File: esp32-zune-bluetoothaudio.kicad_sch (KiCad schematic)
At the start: 21 parts

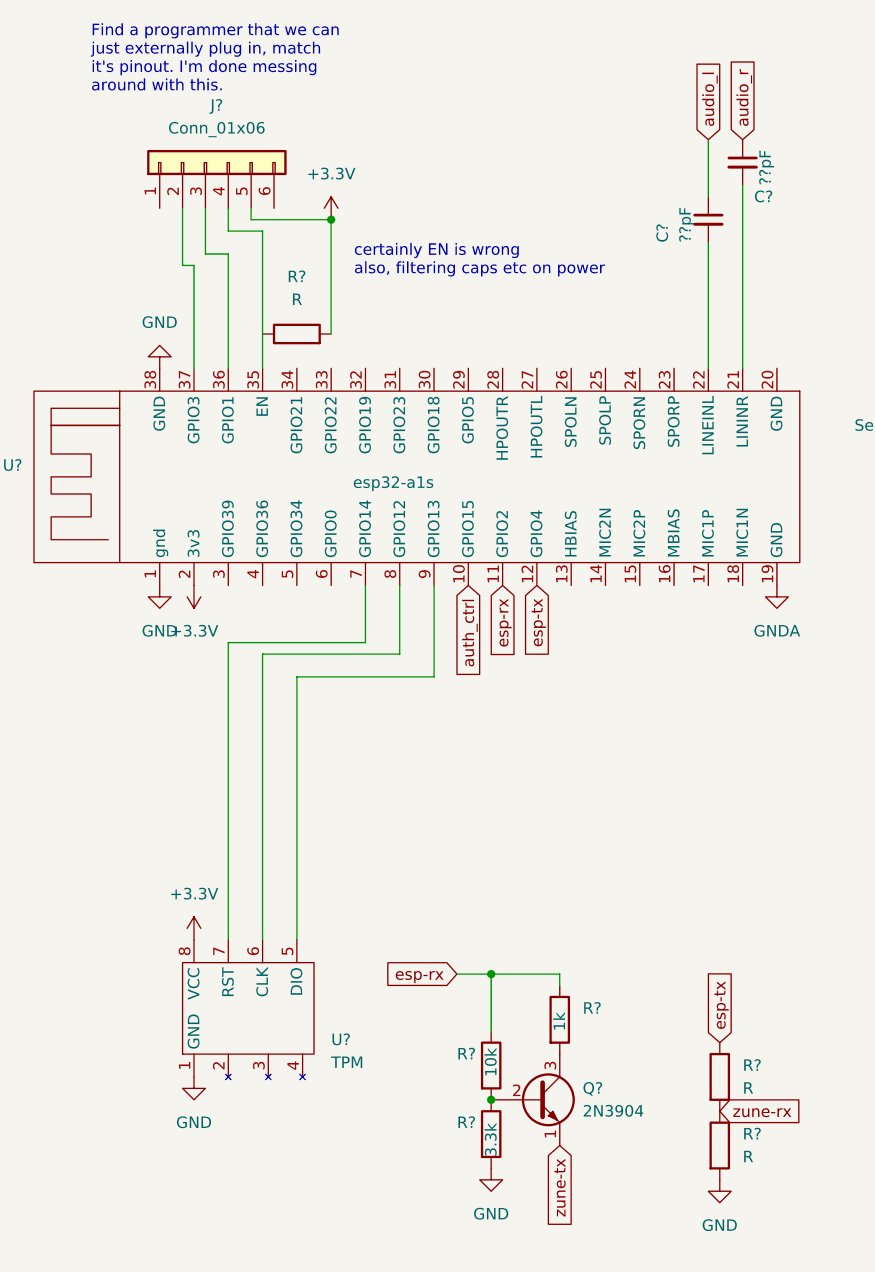
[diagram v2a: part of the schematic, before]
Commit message: starting to write a zune "driver", updating schematic to match breadboard. I'm getting close to laying out a pcb.
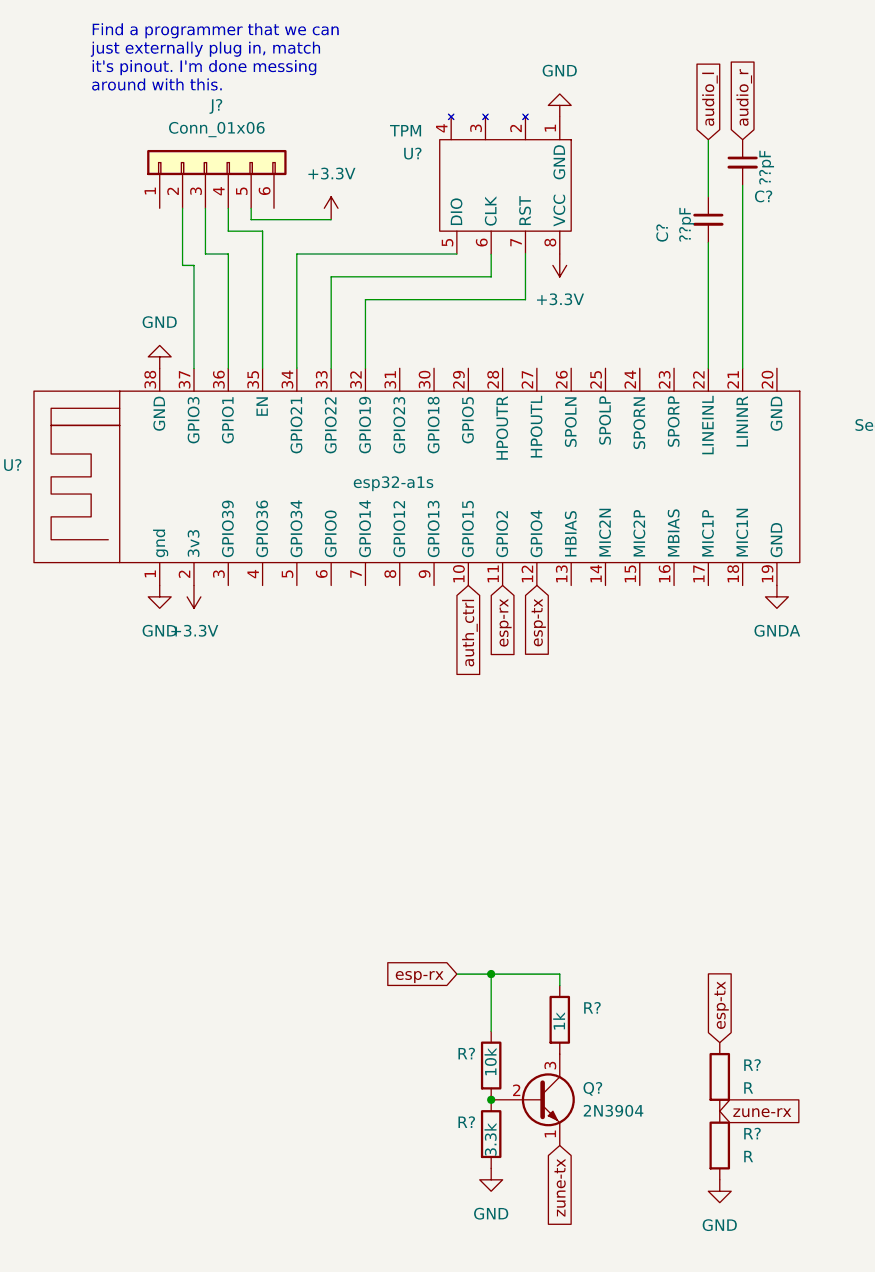
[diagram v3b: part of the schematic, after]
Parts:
- removed R?: R, symbol Device:R
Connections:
- net at U?.5 (DIO): now also U?.34 (GPIO21); no longer U?.9 (GPIO13)
- net at U?.6 (CLK): now also U?.33 (GPIO22); no longer U?.8 (GPIO12)
- net at U?.7 (RST): now also U?.32 (GPIO19); no longer U?.7 (GPIO14)
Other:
- note removed: "certainly EN is wrong also, filtering caps etc on power"
- moved on the sheet: U?
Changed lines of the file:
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@@
   (junction (at 142.24 115.57) (diameter 0) (color 0 0 0 0)
   )
-  (junction (at 52.07 41.91) (diameter 0) (color 0 0 0 0)
-  )
   (junction (at 233.68 101.6) (diameter 0) (color 0 0 0 0)
   )
   (junction (at 232.41 99.06) (diameter 0) (color 0 0 0 0)
   )
-  (wire (pts (xy 52.07 41.91) (xy 52.07 54.61))
-    (stroke (width 0) (type default) (color 0 0 0 0))
-  )
   (wire (pts (xy 69.85 125.73) (xy 69.85 132.08))
     (stroke (width 0) (type default) (color 0 0 0 0))
@@
     (stroke (width 0) (type default) (color 0 0 0 0))
   )
-  (wire (pts (xy 55.88 88.9) (xy 40.64 88.9))
-    (stroke (width 0) (type default) (color 0 0 0 0))
-  )
-  (wire (pts (xy 48.26 121.92) (xy 48.26 92.71))
+  (wire (pts (xy 69.85 48.26) (xy 52.07 48.26))
     (stroke (width 0) (type default) (color 0 0 0 0))
   )
@@
     (stroke (width 0) (type default) (color 0 0 0 0))
   )
-  (wire (pts (xy 44.45 90.17) (xy 59.69 90.17))
-    (stroke (width 0) (type default) (color 0 0 0 0))
-  )
-  (wire (pts (xy 55.88 82.55) (xy 55.88 88.9))
-    (stroke (width 0) (type default) (color 0 0 0 0))
-  )
   (wire (pts (xy 166.37 45.72) (xy 173.99 45.72))
     (stroke (width 0) (type default) (color 0 0 0 0))
@@
     (stroke (width 0) (type default) (color 0 0 0 0))
   )
+  (wire (pts (xy 73.66 50.8) (xy 55.88 50.8))
+    (stroke (width 0) (type default) (color 0 0 0 0))
+  )
   (wire (pts (xy 234.95 43.18) (xy 233.68 43.18))
     (stroke (width 0) (type default) (color 0 0 0 0))
   )
+  (wire (pts (xy 48.26 45.72) (xy 48.26 58.42))
+    (stroke (width 0) (type default) (color 0 0 0 0))
+  )
   (wire (pts (xy 217.17 88.9) (xy 217.17 91.44))
     (stroke (width 0) (type default) (color 0 0 0 0))
@@
     (stroke (width 0) (type default) (color 0 0 0 0))
   )
-  (wire (pts (xy 48.26 92.71) (xy 63.5 92.71))
+  (wire (pts (xy 55.88 50.8) (xy 55.88 58.42))
     (stroke (width 0) (type default) (color 0 0 0 0))
   )
@@
     (stroke (width 0) (type default) (color 0 0 0 0))
   )
-  (wire (pts (xy 59.69 90.17) (xy 59.69 82.55))
+  (wire (pts (xy 66.04 45.72) (xy 48.26 45.72))
     (stroke (width 0) (type default) (color 0 0 0 0))
   )
@@
     (stroke (width 0) (type default) (color 0 0 0 0))
   )
+  (wire (pts (xy 69.85 45.72) (xy 69.85 48.26))
+    (stroke (width 0) (type default) (color 0 0 0 0))
+  )
   (wire (pts (xy 228.6 45.72) (xy 228.6 48.26))
     (stroke (width 0) (type default) (color 0 0 0 0))
@@
     (stroke (width 0) (type default) (color 0 0 0 0))
   )
-  (wire (pts (xy 63.5 92.71) (xy 63.5 82.55))
-    (stroke (width 0) (type default) (color 0 0 0 0))
-  )
   (wire (pts (xy 44.45 43.18) (xy 40.64 43.18))
     (stroke (width 0) (type default) (color 0 0 0 0))
@@
     (stroke (width 0) (type default) (color 0 0 0 0))
   )
-  (wire (pts (xy 44.45 121.92) (xy 44.45 90.17))
-    (stroke (width 0) (type default) (color 0 0 0 0))
-  )
   (wire (pts (xy 233.68 101.6) (xy 232.41 101.6))
     (stroke (width 0) (type default) (color 0 0 0 0))
@@
     (stroke (width 0) (type default) (color 0 0 0 0))
   )
-  (wire (pts (xy 40.64 88.9) (xy 40.64 121.92))
+  (wire (pts (xy 73.66 45.72) (xy 73.66 50.8))
     (stroke (width 0) (type default) (color 0 0 0 0))
   )
@@
     (stroke (width 0) (type default) (color 0 0 0 0))
   )
+  (wire (pts (xy 52.07 48.26) (xy 52.07 58.42))
+    (stroke (width 0) (type default) (color 0 0 0 0))
+  )
   (wire (pts (xy 36.83 58.42) (xy 36.83 46.99))
     (stroke (width 0) (type default) (color 0 0 0 0))
@@
   (wire (pts (xy 234.95 101.6) (xy 233.68 101.6))
     (stroke (width 0) (type default) (color 0 0 0 0))
-  )
-  (text "certainly EN is wrong\nalso, filtering caps etc on power"
-    (at 54.61 48.26 0)
-    (effects (font (size 1.27 1.27)) (justify left bottom))
   )
   (text "Find a programmer that we can \njust externally plug in, match\nit's pinout. I'm done messing \naround with this."
@@
     (pin "2")
   )
-  (symbol (lib_id "power:+3.3V") (at 36.83 121.92 0) (unit 1)
-    (in_bom yes) (on_board yes) (fields_autoplaced)
-    (property "Reference" "#PWR?" (id 0) (at 36.83 125.73 0)
-      (effects (font (size 1.27 1.27)) hide)
-    )
-    (property "Value" "+3.3V" (id 1) (at 36.83 116.84 0))
-    (property "Footprint" "" (id 2) (at 36.83 121.92 0)
-      (effects (font (size 1.27 1.27)) hide)
-    )
-    (property "Datasheet" "" (id 3) (at 36.83 121.92 0)
+  (symbol (lib_id "power:+3.3V") (at 77.47 45.72 180) (unit 1)
+    (in_bom yes) (on_board yes)
+    (property "Reference" "#PWR?" (id 0) (at 77.47 41.91 0)
+      (effects (font (size 1.27 1.27)) hide)
+    )
+    (property "Value" "+3.3V" (id 1) (at 77.47 50.8 0))
+    (property "Footprint" "" (id 2) (at 77.47 45.72 0)
+      (effects (font (size 1.27 1.27)) hide)
+    )
+    (property "Datasheet" "" (id 3) (at 77.47 45.72 0)
       (effects (font (size 1.27 1.27)) hide)
     )
@@
     (pin "3")
   )
-  (symbol (lib_id "Device:R") (at 48.26 54.61 90) (unit 1)
-    (in_bom yes) (on_board yes) (fields_autoplaced)
-    (property "Reference" "R?" (id 0) (at 48.26 48.26 90))
-    (property "Value" "R" (id 1) (at 48.26 50.8 90))
-    (property "Footprint" "" (id 2) (at 48.26 56.388 90)
-      (effects (font (size 1.27 1.27)) hide)
-    )
-    (property "Datasheet" "~" (id 3) (at 48.26 54.61 0)
-      (effects (font (size 1.27 1.27)) hide)
-    )
-    (pin "1")
-    (pin "2")
-  )
-  (symbol (lib_id "esp32-zune-bluetoothaudio:TPM") (at 43.18 130.81 90) (unit 1)
-    (in_bom yes) (on_board yes) (fields_autoplaced)
-    (property "Reference" "U?" (id 0) (at 52.07 133.0324 90)
+  (symbol (lib_id "esp32-zune-bluetoothaudio:TPM") (at 71.12 36.83 270) (unit 1)
+    (in_bom yes) (on_board yes) (fields_autoplaced)
+    (property "Reference" "U?" (id 0) (at 62.23 34.6076 90)
       (effects (font (size 1.27 1.27)) (justify right))
     )
-    (property "Value" "TPM" (id 1) (at 52.07 135.5724 90)
+    (property "Value" "TPM" (id 1) (at 62.23 32.0676 90)
       (effects (font (size 1.27 1.27)) (justify right))
     )
-    (property "Footprint" "" (id 2) (at 43.18 130.81 0)
-      (effects (font (size 1.27 1.27)) hide)
-    )
-    (property "Datasheet" "" (id 3) (at 43.18 130.81 0)
+    (property "Footprint" "" (id 2) (at 71.12 36.83 0)
+      (effects (font (size 1.27 1.27)) hide)
+    )
+    (property "Datasheet" "" (id 3) (at 71.12 36.83 0)
       (effects (font (size 1.27 1.27)) hide)
     )
@@
     (pin "2")
   )
-  (symbol (lib_id "power:GND") (at 36.83 137.16 0) (unit 1)
-    (in_bom yes) (on_board yes) (fields_autoplaced)
-    (property "Reference" "#PWR?" (id 0) (at 36.83 143.51 0)
-      (effects (font (size 1.27 1.27)) hide)
-    )
-    (property "Value" "GND" (id 1) (at 36.83 142.24 0))
-    (property "Footprint" "" (id 2) (at 36.83 137.16 0)
-      (effects (font (size 1.27 1.27)) hide)
-    )
-    (property "Datasheet" "" (id 3) (at 36.83 137.16 0)
+  (symbol (lib_id "power:GND") (at 77.47 30.48 180) (unit 1)
+    (in_bom yes) (on_board yes) (fields_autoplaced)
+    (property "Reference" "#PWR?" (id 0) (at 77.47 24.13 0)
+      (effects (font (size 1.27 1.27)) hide)
+    )
+    (property "Value" "GND" (id 1) (at 77.47 25.4 0))
+    (property "Footprint" "" (id 2) (at 77.47 30.48 0)
+      (effects (font (size 1.27 1.27)) hide)
+    )
+    (property "Datasheet" "" (id 3) (at 77.47 30.48 0)
       (effects (font (size 1.27 1.27)) hide)
     )
@@
       (reference "R?") (unit 1) (value "5.1k") (footprint "")
     )
-    (path "/6e0a5e0c-fe95-4f96-a7d3-ae4f8b21eb7d"
-      (reference "R?") (unit 1) (value "R") (footprint "")
-    )
     (path "/9b964513-9d48-4617-8831-9ae5380671a8"
